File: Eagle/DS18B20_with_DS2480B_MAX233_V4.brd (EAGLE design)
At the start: 40 x 50 mm, 15 parts, among them IC1 MAX233AEWP, IC2 DS2480B, IC3 DS18B20, IC4 MAX9940

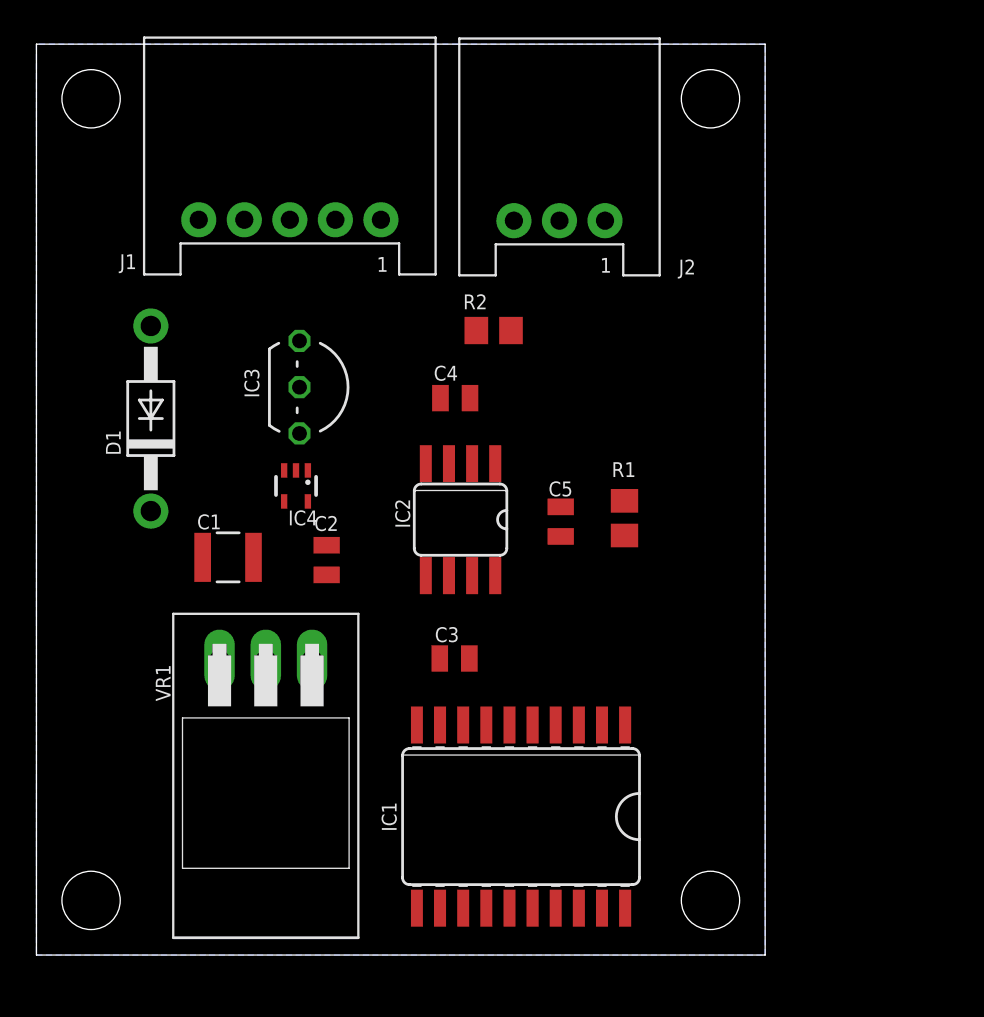
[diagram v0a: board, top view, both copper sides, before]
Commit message: Completely new board layout
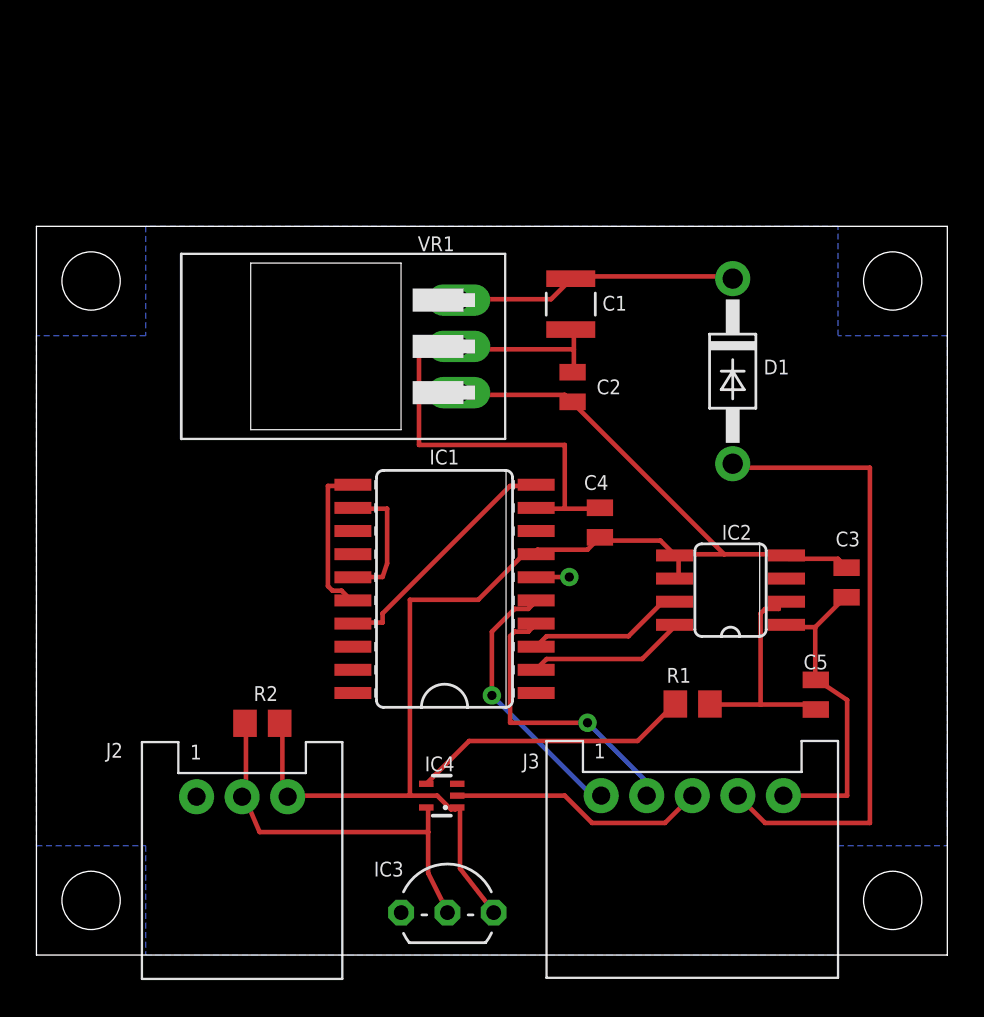
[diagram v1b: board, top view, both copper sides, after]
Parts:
- removed J1: (no value), AU2016:DF1B-5P
- added J3: (no value), AU2016:DF1B-5P
- moved J2 42.9 mm to (11.3, 4.88), turned to 180 degrees
- moved D1 32.0 mm to (38.2, 32.0), turned to 270 degrees
- moved IC3 30.0 mm to (22.6, 2.33), turned to 0 degrees
- moved VR1 27.4 mm to (13.0, 33.4), turned to 90 degrees
- moved R2 25.0 mm to (12.4, 12.7), turned to 0 degrees
- moved C1 23.4 mm to (29.3, 35.7), turned to 270 degrees
- moved C3 21.9 mm to (44.5, 20.4), turned to 270 degrees
- moved IC4 18.8 mm to (22.2, 8.75), turned to 90 degrees
- moved C5 16.9 mm to (42.8, 14.3)
- moved C2 16.5 mm to (29.4, 31.2)
- moved IC2 15.3 mm to (38.1, 20.0), turned to 90 degrees
- moved IC1 13.2 mm to (22.4, 20.1), turned to 90 degrees
- moved R1 10.9 mm to (36.0, 13.8), turned to 180 degrees
- moved C4 10.5 mm to (30.9, 23.7), turned to 90 degrees
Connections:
- net GND: now also J3.P$3, J3.P$5; no longer J1.P$1, J1.P$3
- net N$1: now also J3.P$4; no longer J1.P$2
- net N$4: now also J3.P$1; no longer J1.P$5
- net N$5: now also J3.P$2; no longer J1.P$4
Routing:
- net 5V: track 0.00 -> 77.3 mm
- net GND: track 0.00 -> 65.1 mm, vias 0 -> 1
- net N$1: track 0.00 -> 35.1 mm
- net N$14: track 0.00 -> 21.7 mm
- net N$5: track 0.00 -> 16.1 mm, vias 0 -> 1
- net N$2: track 0.00 -> 15.6 mm
- net N$13: track 0.00 -> 15.5 mm
- net N$4: track 0.00 -> 14.9 mm, vias 0 -> 1
- net N$9: track 0.00 -> 13.5 mm
- net N$11: track 0.00 -> 13.1 mm
- net N$10: track 0.00 -> 8.68 mm
- net N$3: track 0.00 -> 8.68 mm
- net N$8: track 0.00 -> 8.57 mm
- net N$7: track 0.00 -> 7.31 mm
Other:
- board size 40 x 50 mm -> 50 x 40 mm

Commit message: Design with MAX9940 protection
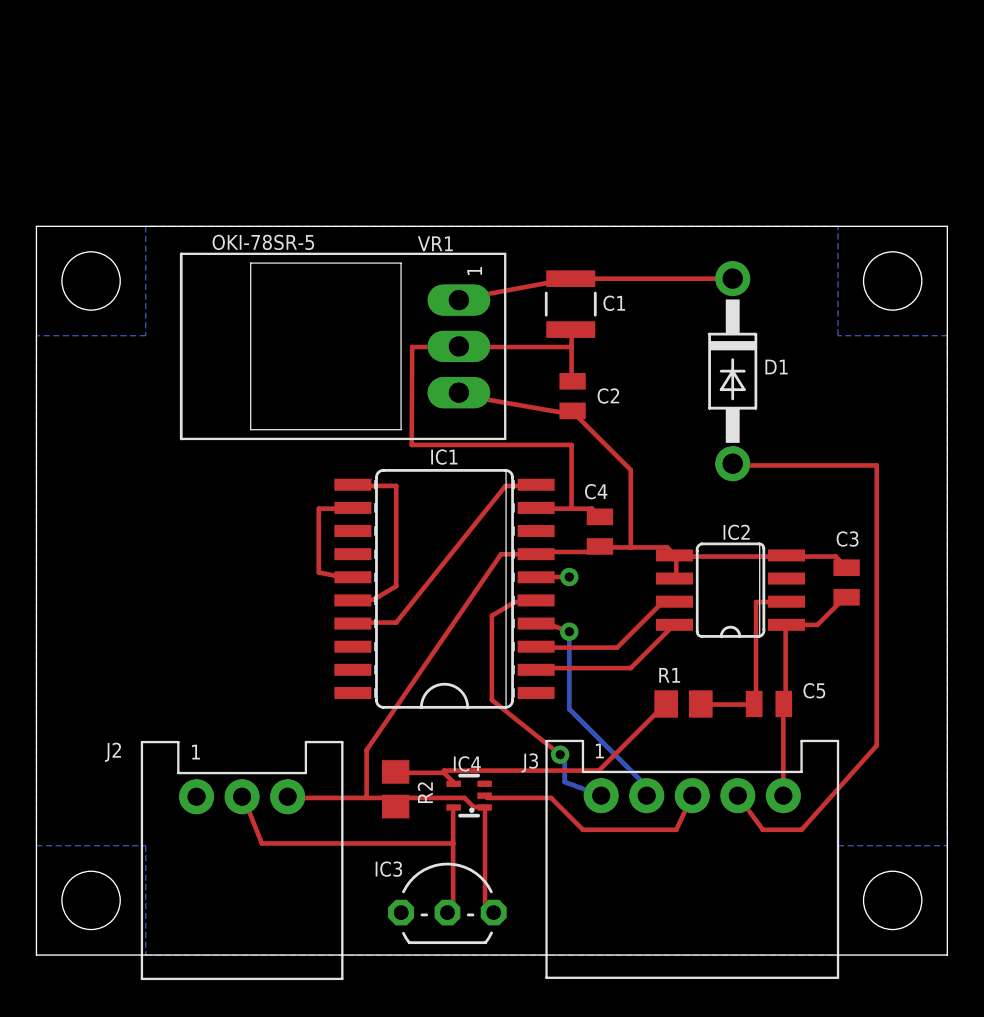
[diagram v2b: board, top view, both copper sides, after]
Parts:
- moved R2 8.17 mm to (19.7, 9.10), turned to 270 degrees
- moved C5 2.62 mm to (40.2, 13.8), turned to 0 degrees
- moved IC4 1.50 mm to (23.8, 8.75)
- moved C2 0.50 mm to (29.4, 30.7)
- moved C4 0.50 mm to (30.9, 23.2)
- moved R1 0.50 mm to (35.5, 13.8)
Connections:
- net N$13: now also R2.1
- net N$14: no longer R2.1
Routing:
- net 5V: track 77.3 -> 70.3 mm
- net GND: track 65.1 -> 61.6 mm
- net N$5: track 16.1 -> 12.7 mm
- net N$11: track 13.1 -> 10.3 mm
- net N$14: track 21.7 -> 19.4 mm
- net N$8: track 8.57 -> 10.6 mm
- net N$13: track 15.5 -> 17.3 mm
- net N$1: track 35.1 -> 34.0 mm
- net N$4: track 14.9 -> 16.0 mm
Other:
- board text added: "+5V"
- board text added: "2016-02-01 1-Wire to RS-232 Converter"
- board text removed: "2015-12-18 1-Wire to RS-232 Converter"
